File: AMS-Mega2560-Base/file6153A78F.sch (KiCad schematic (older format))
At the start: 12 parts, among them Q2 IRF510, Q3 IRF510, Q4 IRF510, Q5 2N7000, Q6 2N7000

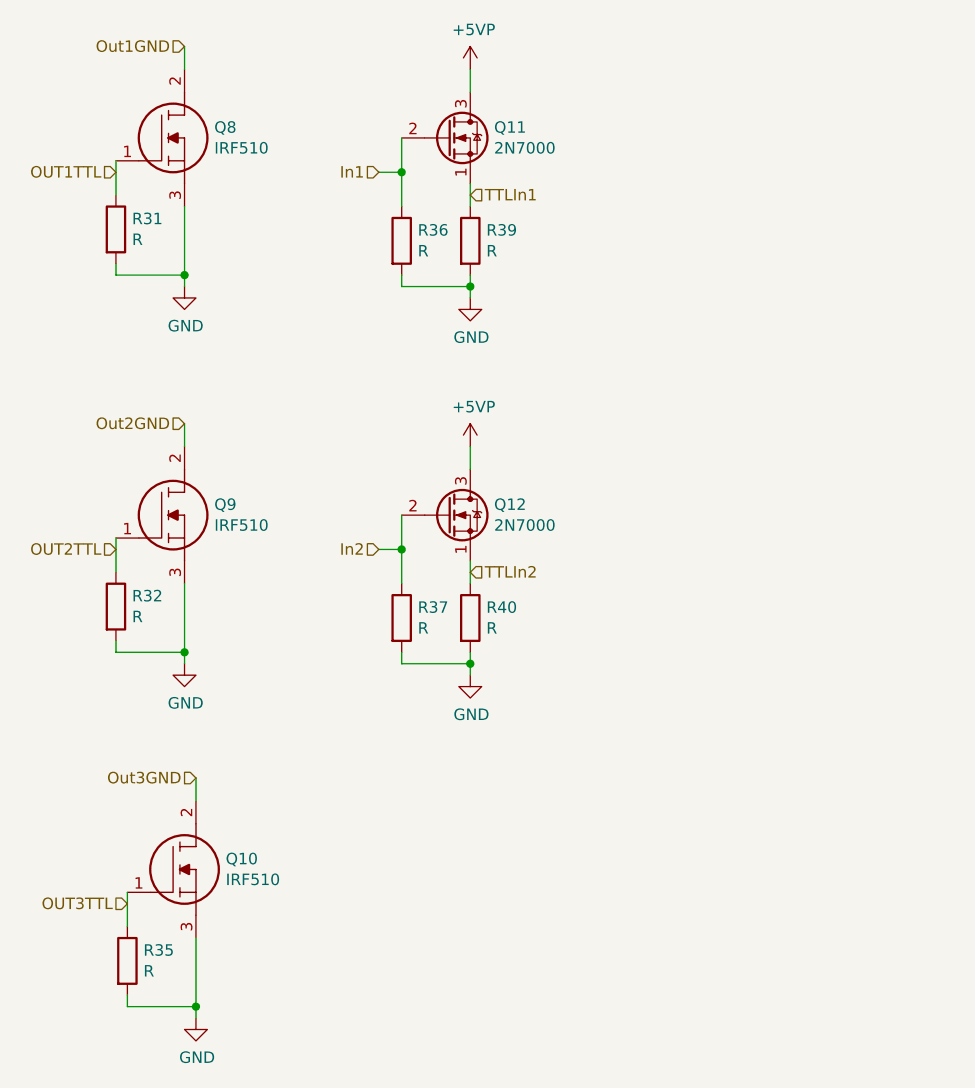
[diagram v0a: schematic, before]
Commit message: rearranging some of the hw design before i rename the repo.
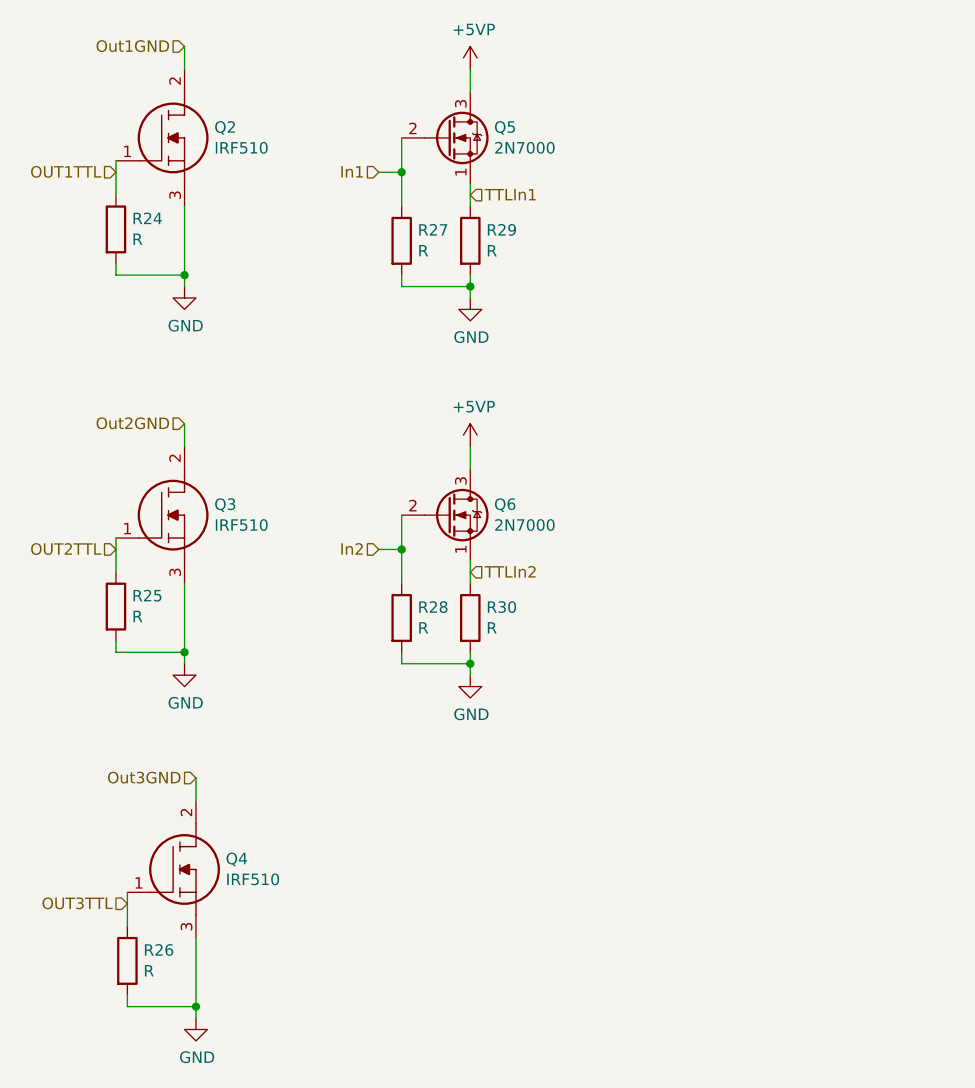
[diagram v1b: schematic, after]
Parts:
- renumbered Q4 to Q3, Q3 to Q4, R20 to R24, R21 to R25
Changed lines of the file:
@@
 $Descr A4 11693 8268
 encoding utf-8
-Sheet 12 13
+Sheet 12 14
 Title ""
 Date ""
@@
 $EndDescr
 $Comp
-L SamacSys_Parts:IRF510 Q3
+L SamacSys_Parts:IRF510 Q?
 U 1 1 6151FB60
 P 4300 5150
-AR Path="/6153A790/6151FB60" Ref="Q3"  Part="1"
-AR Path="/623D3962/6151FB60" Ref="Q10"  Part="1"
-F 0 "Q10" H 4730 5296 50  0000 L CNN
+AR Path="/6153A790/6151FB60" Ref="Q?"  Part="1"
+AR Path="/623D3962/6151FB60" Ref="Q4"  Part="1"
+F 0 "Q4" H 4730 5296 50  0000 L CNN
 F 1 "IRF510" H 4730 5205 50  0000 L CNN
 F 2 "SamacSys_Parts:TO254P465X1024X2050-3P" H 4750 5100 50  0001 L CNN
@@
 $EndComp
 $Comp
-L Device:R R26
+L Device:R R?
 U 1 1 615214D0
 P 4300 5450
-AR Path="/6153A790/615214D0" Ref="R26"  Part="1"
-AR Path="/623D3962/615214D0" Ref="R35"  Part="1"
-F 0 "R35" H 4370 5496 50  0000 L CNN
+AR Path="/6153A790/615214D0" Ref="R?"  Part="1"
+AR Path="/623D3962/615214D0" Ref="R26"  Part="1"
+F 0 "R26" H 4370 5496 50  0000 L CNN
 F 1 "R" H 4370 5405 50  0000 L CNN
 F 2 "Resistor_THT:R_Axial_DIN0207_L6.3mm_D2.5mm_P5.08mm_Vertical" V 4230 5450 50  0001 C CNN
@@
 	4600 5700 4600 5650
 $Comp
-L power:GND #PWR090
+L power:GND #PWR?
 U 1 1 615214D7
 P 4600 5700
-AR Path="/6153A790/615214D7" Ref="#PWR090"  Part="1"
-AR Path="/623D3962/615214D7" Ref="#PWR092"  Part="1"
-F 0 "#PWR092" H 4600 5450 50  0001 C CNN
+AR Path="/6153A790/615214D7" Ref="#PWR?"  Part="1"
+AR Path="/623D3962/615214D7" Ref="#PWR097"  Part="1"
+F 0 "#PWR097" H 4600 5450 50  0001 C CNN
 F 1 "GND" H 4605 5527 50  0000 C CNN
 F 2 "" H 4600 5700 50  0001 C CNN
@@
 	4600 4750 4600 4650
 $Comp
-L SamacSys_Parts:IRF510 Q4
+L SamacSys_Parts:IRF510 Q?
 U 1 1 623FCDC8
 P 4250 3600
-AR Path="/6153A790/623FCDC8" Ref="Q4"  Part="1"
-AR Path="/623D3962/623FCDC8" Ref="Q9"  Part="1"
-F 0 "Q9" H 4680 3746 50  0000 L CNN
+AR Path="/6153A790/623FCDC8" Ref="Q?"  Part="1"
+AR Path="/623D3962/623FCDC8" Ref="Q3"  Part="1"
+F 0 "Q3" H 4680 3746 50  0000 L CNN
 F 1 "IRF510" H 4680 3655 50  0000 L CNN
 F 2 "SamacSys_Parts:TO254P465X1024X2050-3P" H 4700 3550 50  0001 L CNN
@@
 $EndComp
 $Comp
-L Device:R R21
+L Device:R R?
 U 1 1 623FCDCE
 P 4250 3900
-AR Path="/6153A790/623FCDCE" Ref="R21"  Part="1"
-AR Path="/623D3962/623FCDCE" Ref="R32"  Part="1"
-F 0 "R32" H 4320 3946 50  0000 L CNN
+AR Path="/6153A790/623FCDCE" Ref="R?"  Part="1"
+AR Path="/623D3962/623FCDCE" Ref="R25"  Part="1"
+F 0 "R25" H 4320 3946 50  0000 L CNN
 F 1 "R" H 4320 3855 50  0000 L CNN
 F 2 "Resistor_THT:R_Axial_DIN0207_L6.3mm_D2.5mm_P5.08mm_Vertical" V 4180 3900 50  0001 C CNN
@@
 	4550 4150 4550 4100
 $Comp
-L power:GND #PWR071
+L power:GND #PWR?
 U 1 1 623FCDD5
 P 4550 4150
-AR Path="/6153A790/623FCDD5" Ref="#PWR071"  Part="1"
-AR Path="/623D3962/623FCDD5" Ref="#PWR091"  Part="1"
-F 0 "#PWR091" H 4550 3900 50  0001 C CNN
+AR Path="/6153A790/623FCDD5" Ref="#PWR?"  Part="1"
+AR Path="/623D3962/623FCDD5" Ref="#PWR096"  Part="1"
+F 0 "#PWR096" H 4550 3900 50  0001 C CNN
 F 1 "GND" H 4555 3977 50  0000 C CNN
 F 2 "" H 4550 4150 50  0001 C CNN
@@
 	4550 3200 4550 3100
 $Comp
-L Transistor_FET:2N7000 Q6
+L Transistor_FET:2N7000 Q?
 U 1 1 623FCDE3
 P 5700 3500
-AR Path="/6153A790/623FCDE3" Ref="Q6"  Part="1"
-AR Path="/623D3962/623FCDE3" Ref="Q12"  Part="1"
-F 0 "Q12" H 5904 3546 50  0000 L CNN
+AR Path="/6153A790/623FCDE3" Ref="Q?"  Part="1"
+AR Path="/623D3962/623FCDE3" Ref="Q6"  Part="1"
+F 0 "Q6" H 5904 3546 50  0000 L CNN
 F 1 "2N7000" H 5904 3455 50  0000 L CNN
 F 2 "Package_TO_SOT_THT:TO-92_Inline" H 5900 3425 50  0001 L CIN
@@
 $EndComp
 $Comp
-L Device:R R30
+L Device:R R?
 U 1 1 623FCDE9
 P 5800 3950
-AR Path="/6153A790/623FCDE9" Ref="R30"  Part="1"
-AR Path="/623D3962/623FCDE9" Ref="R40"  Part="1"
-F 0 "R40" H 5870 3996 50  0000 L CNN
+AR Path="/6153A790/623FCDE9" Ref="R?"  Part="1"
+AR Path="/623D3962/623FCDE9" Ref="R30"  Part="1"
+F 0 "R30" H 5870 3996 50  0000 L CNN
 F 1 "R" H 5870 3905 50  0000 L CNN
 F 2 "Resistor_THT:R_Axial_DIN0207_L6.3mm_D2.5mm_P5.08mm_Vertical" V 5730 3950 50  0001 C CNN
@@
 $EndComp
 $Comp
-L Device:R R28
+L Device:R R?
 U 1 1 623FCDEF
 P 5500 3950
-AR Path="/6153A790/623FCDEF" Ref="R28"  Part="1"
-AR Path="/623D3962/623FCDEF" Ref="R37"  Part="1"
-F 0 "R37" H 5570 3996 50  0000 L CNN
+AR Path="/6153A790/623FCDEF" Ref="R?"  Part="1"
+AR Path="/623D3962/623FCDEF" Ref="R28"  Part="1"
+F 0 "R28" H 5570 3996 50  0000 L CNN
 F 1 "R" H 5570 3905 50  0000 L CNN
 F 2 "Resistor_THT:R_Axial_DIN0207_L6.3mm_D2.5mm_P5.08mm_Vertical" V 5430 3950 50  0001 C CNN
@@
 	5800 4200 5800 4150
 $Comp
-L power:GND #PWR088
+L power:GND #PWR?
 U 1 1 623FCDF6
 P 5800 4200
-AR Path="/6153A790/623FCDF6" Ref="#PWR088"  Part="1"
-AR Path="/623D3962/623FCDF6" Ref="#PWR096"  Part="1"
-F 0 "#PWR096" H 5800 3950 50  0001 C CNN
+AR Path="/6153A790/623FCDF6" Ref="#PWR?"  Part="1"
+AR Path="/623D3962/623FCDF6" Ref="#PWR0101"  Part="1"
+F 0 "#PWR0101" H 5800 3950 50  0001 C CNN
 F 1 "GND" H 5805 4027 50  0000 C CNN
 F 2 "" H 5800 4200 50  0001 C CNN
@@
 P 5800 3200
 AR Path="/61493C0E/623FCE08" Ref="#PWR?"  Part="1"
-AR Path="/6153A790/623FCE08" Ref="#PWR074"  Part="1"
-AR Path="/623D3962/623FCE08" Ref="#PWR095"  Part="1"
-F 0 "#PWR095" H 5800 3050 50  0001 C CNN
+AR Path="/6153A790/623FCE08" Ref="#PWR?"  Part="1"
+AR Path="/623D3962/623FCE08" Ref="#PWR0100"  Part="1"
+F 0 "#PWR0100" H 5800 3050 50  0001 C CNN
 F 1 "+5VP" H 5815 3373 50  0000 C CNN
 F 2 "" H 5800 3200 50  0001 C CNN
@@
 $EndComp
 $Comp
-L SamacSys_Parts:IRF510 Q2
+L SamacSys_Parts:IRF510 Q?
 U 1 1 623FFB6C
 P 4250 1950
-AR Path="/6153A790/623FFB6C" Ref="Q2"  Part="1"
-AR Path="/623D3962/623FFB6C" Ref="Q8"  Part="1"
-F 0 "Q8" H 4680 2096 50  0000 L CNN
+AR Path="/6153A790/623FFB6C" Ref="Q?"  Part="1"
+AR Path="/623D3962/623FFB6C" Ref="Q2"  Part="1"
+F 0 "Q2" H 4680 2096 50  0000 L CNN
 F 1 "IRF510" H 4680 2005 50  0000 L CNN
 F 2 "SamacSys_Parts:TO254P465X1024X2050-3P" H 4700 1900 50  0001 L CNN
@@
 $EndComp
 $Comp
-L Device:R R20
+L Device:R R?
 U 1 1 623FFB72
 P 4250 2250
-AR Path="/6153A790/623FFB72" Ref="R20"  Part="1"
-AR Path="/623D3962/623FFB72" Ref="R31"  Part="1"
-F 0 "R31" H 4320 2296 50  0000 L CNN
+AR Path="/6153A790/623FFB72" Ref="R?"  Part="1"
+AR Path="/623D3962/623FFB72" Ref="R24"  Part="1"
+F 0 "R24" H 4320 2296 50  0000 L CNN
 F 1 "R" H 4320 2205 50  0000 L CNN
 F 2 "Resistor_THT:R_Axial_DIN0207_L6.3mm_D2.5mm_P5.08mm_Vertical" V 4180 2250 50  0001 C CNN
@@
 	4550 2500 4550 2450
 $Comp
-L power:GND #PWR070
+L power:GND #PWR?
 U 1 1 623FFB79
 P 4550 2500
-AR Path="/6153A790/623FFB79" Ref="#PWR070"  Part="1"
-AR Path="/623D3962/623FFB79" Ref="#PWR089"  Part="1"
-F 0 "#PWR089" H 4550 2250 50  0001 C CNN
+AR Path="/6153A790/623FFB79" Ref="#PWR?"  Part="1"
+AR Path="/623D3962/623FFB79" Ref="#PWR095"  Part="1"
+F 0 "#PWR095" H 4550 2250 50  0001 C CNN
 F 1 "GND" H 4555 2327 50  0000 C CNN
 F 2 "" H 4550 2500 50  0001 C CNN
@@
 	4550 1550 4550 1450
 $Comp
-L Transistor_FET:2N7000 Q5
+L Transistor_FET:2N7000 Q?
 U 1 1 623FFB87
 P 5700 1850
-AR Path="/6153A790/623FFB87" Ref="Q5"  Part="1"
-AR Path="/623D3962/623FFB87" Ref="Q11"  Part="1"
-F 0 "Q11" H 5904 1896 50  0000 L CNN
+AR Path="/6153A790/623FFB87" Ref="Q?"  Part="1"
+AR Path="/623D3962/623FFB87" Ref="Q5"  Part="1"
+F 0 "Q5" H 5904 1896 50  0000 L CNN
 F 1 "2N7000" H 5904 1805 50  0000 L CNN
 F 2 "Package_TO_SOT_THT:TO-92_Inline" H 5900 1775 50  0001 L CIN
@@
 $EndComp
 $Comp
-L Device:R R29
+L Device:R R?
 U 1 1 623FFB8D
 P 5800 2300
-AR Path="/6153A790/623FFB8D" Ref="R29"  Part="1"
-AR Path="/623D3962/623FFB8D" Ref="R39"  Part="1"
-F 0 "R39" H 5870 2346 50  0000 L CNN
+AR Path="/6153A790/623FFB8D" Ref="R?"  Part="1"
+AR Path="/623D3962/623FFB8D" Ref="R29"  Part="1"
+F 0 "R29" H 5870 2346 50  0000 L CNN
 F 1 "R" H 5870 2255 50  0000 L CNN
 F 2 "Resistor_THT:R_Axial_DIN0207_L6.3mm_D2.5mm_P5.08mm_Vertical" V 5730 2300 50  0001 C CNN
@@
 $EndComp
 $Comp
-L Device:R R27
+L Device:R R?
 U 1 1 623FFB93
 P 5500 2300
-AR Path="/6153A790/623FFB93" Ref="R27"  Part="1"
-AR Path="/623D3962/623FFB93" Ref="R36"  Part="1"
-F 0 "R36" H 5570 2346 50  0000 L CNN
+AR Path="/6153A790/623FFB93" Ref="R?"  Part="1"
+AR Path="/623D3962/623FFB93" Ref="R27"  Part="1"
+F 0 "R27" H 5570 2346 50  0000 L CNN
 F 1 "R" H 5570 2255 50  0000 L CNN
 F 2 "Resistor_THT:R_Axial_DIN0207_L6.3mm_D2.5mm_P5.08mm_Vertical" V 5430 2300 50  0001 C CNN
@@
 	5800 2550 5800 2500
 $Comp
-L power:GND #PWR073
+L power:GND #PWR?
 U 1 1 623FFB9A
 P 5800 2550
-AR Path="/6153A790/623FFB9A" Ref="#PWR073"  Part="1"
-AR Path="/623D3962/623FFB9A" Ref="#PWR094"  Part="1"
-F 0 "#PWR094" H 5800 2300 50  0001 C CNN
+AR Path="/6153A790/623FFB9A" Ref="#PWR?"  Part="1"
+AR Path="/623D3962/623FFB9A" Ref="#PWR099"  Part="1"
+F 0 "#PWR099" H 5800 2300 50  0001 C CNN
 F 1 "GND" H 5805 2377 50  0000 C CNN
 F 2 "" H 5800 2550 50  0001 C CNN
@@
 P 5800 1550
 AR Path="/61493C0E/623FFBAC" Ref="#PWR?"  Part="1"
-AR Path="/6153A790/623FFBAC" Ref="#PWR072"  Part="1"
-AR Path="/623D3962/623FFBAC" Ref="#PWR093"  Part="1"
-F 0 "#PWR093" H 5800 1400 50  0001 C CNN
+AR Path="/6153A790/623FFBAC" Ref="#PWR?"  Part="1"
+AR Path="/623D3962/623FFBAC" Ref="#PWR098"  Part="1"
+F 0 "#PWR098" H 5800 1400 50  0001 C CNN
 F 1 "+5VP" H 5815 1723 50  0000 C CNN
 F 2 "" H 5800 1550 50  0001 C CNN
